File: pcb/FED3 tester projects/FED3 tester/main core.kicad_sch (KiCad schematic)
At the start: 44 parts, among them J2 Conn_02x03_Odd_Even, Q1 DMN63D8L-7, SW1 SW_SPST, SW2 SW_SPST, SW3 SW_SPST, SW4 SW_SPST, SW5 SW_SPST, SW6 SW_SPST, SW7 SW_SPST, SW8 SW_SPST, SW9 SW_SPST, U5 ATXMEGA32A4U-MH

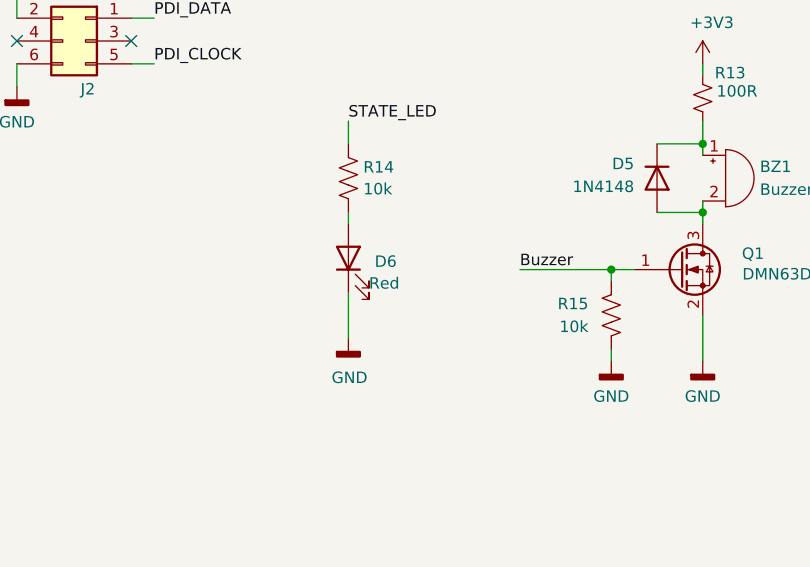
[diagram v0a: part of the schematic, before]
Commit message: State LED - modificada côr para amarelo
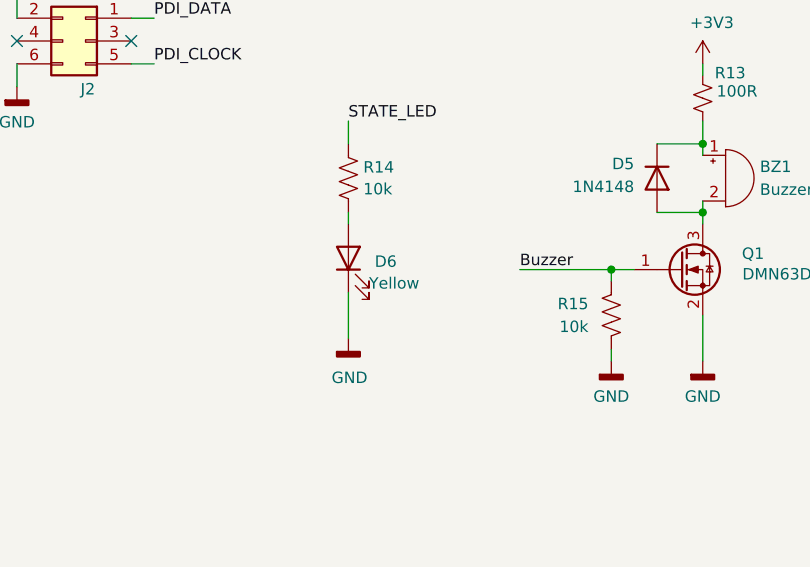
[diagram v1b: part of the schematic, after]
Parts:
- D6: value Red -> Yellow; MPN VFHR1116P-4C82A-TR -> 5990040007F; OEPSPN OEPS030038 -> OEPS030043
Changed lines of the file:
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@@
 			)
 		)
-		(property "Value" "Red"
+		(property "Value" "Yellow"
 			(at 221.996 155.194 90)
 			(show_name no)
@@
 			)
 		)
-		(property "Description" "LED 0603 Red 635nm 20mA"
+		(property "Description" "LED 0603 Yellow 590nm 20mA"
 			(at 219.71 152.4 0)
 			(hide yes)
@@
 			)
 		)
-		(property "MPN" "VFHR1116P-4C82A-TR"
+		(property "MPN" "5990040007F"
 			(at 219.71 152.4 0)
 			(hide yes)
@@
 			)
 		)
-		(property "OEPSPN" "OEPS030038"
+		(property "OEPSPN" "OEPS030043"
 			(at 219.71 152.4 0)
 			(hide yes)

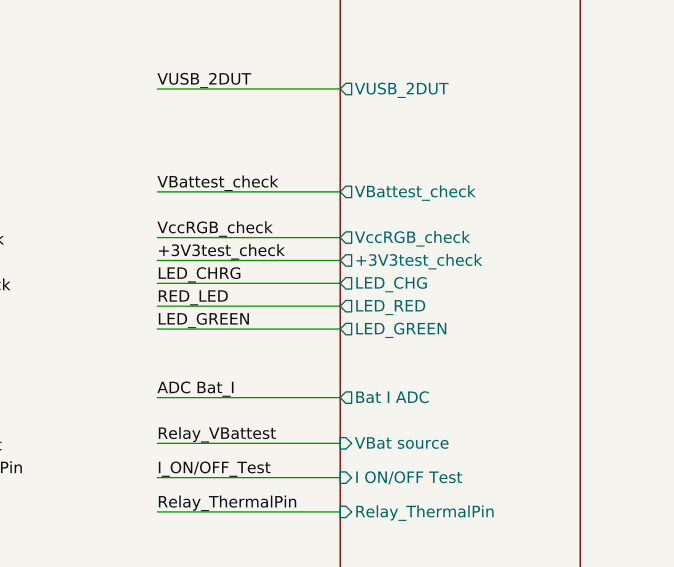
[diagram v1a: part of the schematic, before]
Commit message: completos OEPSPN & MPN
- andar de I-measure  ZXCT1086 redimensionado
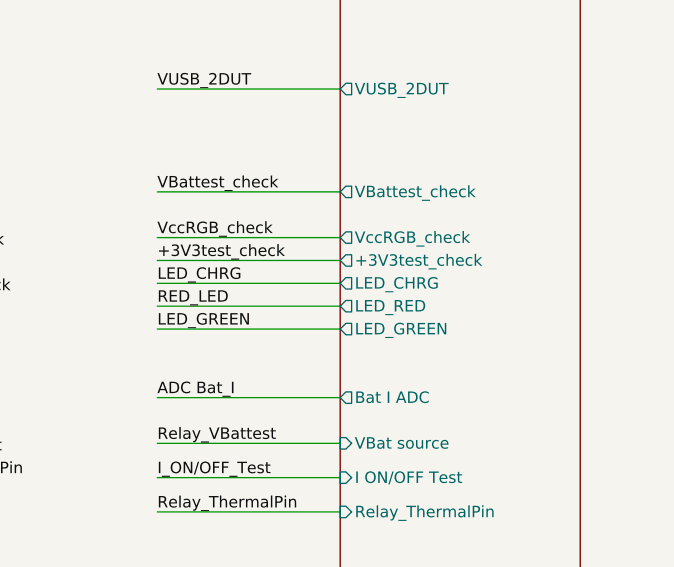
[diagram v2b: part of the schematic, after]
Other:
- sheet DUT stage ports: added LED_CHRG; removed LED_CHG
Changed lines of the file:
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@@
 		(in_bom yes)
 		(on_board yes)
-		(in_pos_files yes)
+		(in_pos_files no)
 		(dnp no)
 		(property "Reference" "J2"
@@
 			)
 		)
-		(pin "LED_CHG" output
+		(pin "LED_CHRG" output
 			(at 241.3 60.96 180)
 			(effects

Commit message: revistos OEPSPN & MPN com gsheet - OK
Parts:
- R14, R17: MPN ERJ-2RKF1002X -> CPF0402B10KE1; OEPSPN OEPS020013 -> OEPS020043; Tolerance 1% -> 0.1%
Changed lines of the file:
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@@
 			)
 		)
-		(property "Description" "SMD 0402 330Ω ±1% 0.200W"
+		(property "Description" "SMD 0402 2kΩ ±1% 0.100W"
 			(at 69.85 71.12 0)
 			(hide yes)
@@
 			)
 		)
-		(property "Description" "SMD 0402 560Ω ±1% 0.063W"
+		(property "Description" "SMD 0402 2kΩ ±1% 0.100W"
 			(at 40.64 38.1 0)
 			(hide yes)
@@
 			)
 		)
-		(property "Description" "SMD 0402 330Ω ±1% 0.200W"
+		(property "Description" "SMD 0402 2kΩ ±1% 0.100W"
 			(at 38.1 71.12 0)
 			(hide yes)
@@
 			)
 		)
-		(property "Description" "SMD 0402 10kΩ ±1% 0.200W"
+		(property "Description" "SMD 0402 10kΩ ±0.1% 0.063W"
 			(at 46.99 185.42 0)
 			(hide yes)
@@
 			)
 		)
-		(property "MPN" "ERJ-2RKF1002X"
+		(property "MPN" "CPF0402B10KE1"
 			(at 43.942 194.183 0)
 			(hide yes)
@@
 			)
 		)
-		(property "OEPSPN" "OEPS020013"
+		(property "OEPSPN" "OEPS020043"
 			(at 46.99 185.42 0)
 			(hide yes)
@@
 			)
 		)
-		(property "Tolerance" "1%"
+		(property "Tolerance" "0.1%"
 			(at 46.99 185.42 0)
 			(hide yes)
@@
 			)
 		)
-		(property "Description" "SMD 0402 10kΩ ±1% 0.200W"
+		(property "Description" "SMD 0402 10kΩ ±0.1% 0.063W"
 			(at 219.71 143.51 0)
 			(hide yes)
@@
 			)
 		)
-		(property "MPN" "ERJ-2RKF1002X"
+		(property "MPN" "CPF0402B10KE1"
 			(at 228.473 146.558 0)
 			(hide yes)
@@
 			)
 		)
-		(property "OEPSPN" "OEPS020013"
+		(property "OEPSPN" "OEPS020043"
 			(at 219.71 143.51 0)
 			(hide yes)
@@
 			)
 		)
-		(property "Tolerance" "1%"
+		(property "Tolerance" "0.1%"
 			(at 219.71 143.51 0)
 			(hide yes)
@@
 			)
 		)
-		(property "Description" "SMD 0402 330Ω ±1% 0.200W"
+		(property "Description" "SMD 0402 2kΩ ±1% 0.100W"
 			(at 46.99 173.99 0)
 			(hide yes)
@@
 			)
 		)
-		(property "Description" "SMD 0402 330Ω ±1% 0.200W"
+		(property "Description" "SMD 0402 2kΩ ±1% 0.100W"
 			(at 39.37 82.55 0)
 			(hide yes)
